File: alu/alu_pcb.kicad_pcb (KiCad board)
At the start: 2 copper layers, 115.6 x 86.4 mm, 56 parts, among them J1 Conn_02x03_Odd_Even, J2 Conn_02x02_Odd_Even, J3 Conn_02x08_Odd_Even, J4 Conn_02x08_Odd_Even, J5 Conn_02x08_Odd_Even, J6 Conn_02x08_Odd_Even, U1 74LS283, U10 74LS386, U11 74LS02, U12 74LS08, U13 74LS08, U14 74LS02, U15 74LS00, U2 74LS283, U3 74LS244, U4 74LS283, U5 74LS244, U6 74LS283, U7 74LS386, U8 74LS386, U9 74LS386

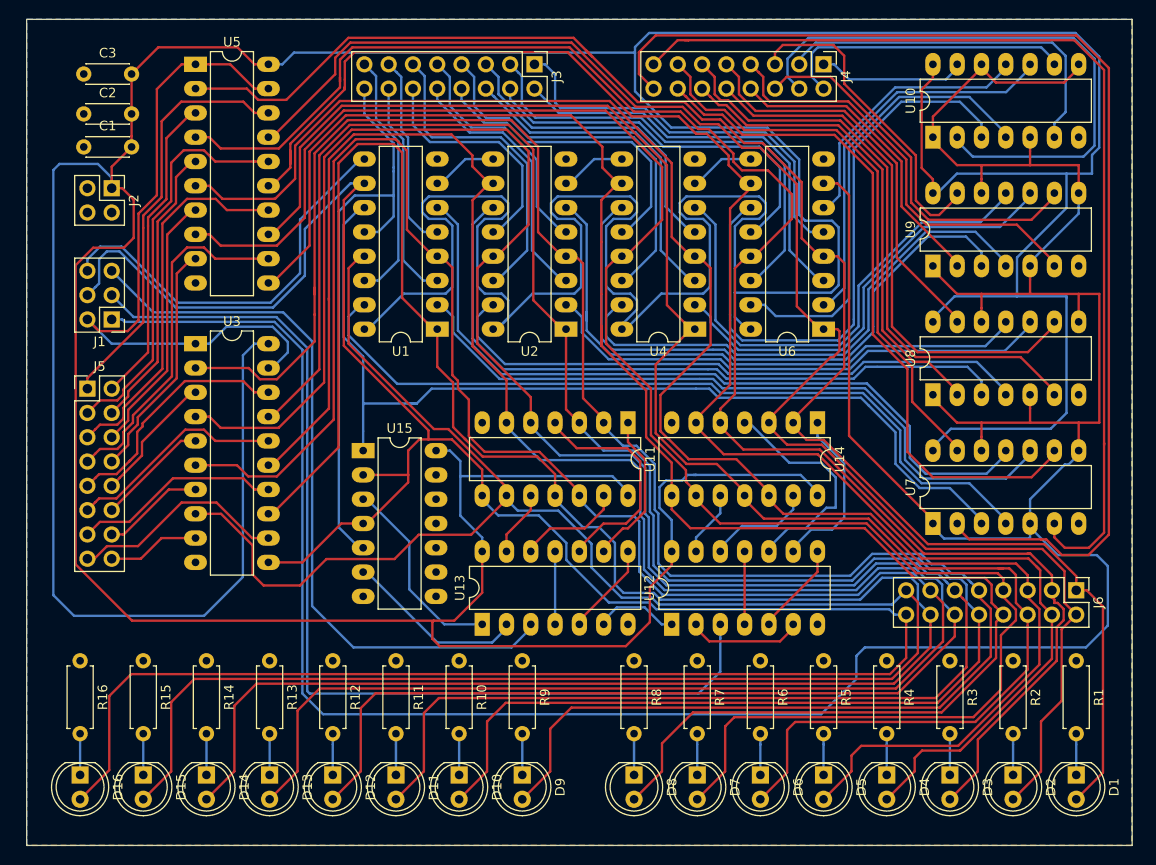
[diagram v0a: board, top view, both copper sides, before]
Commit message: route alu, upde register
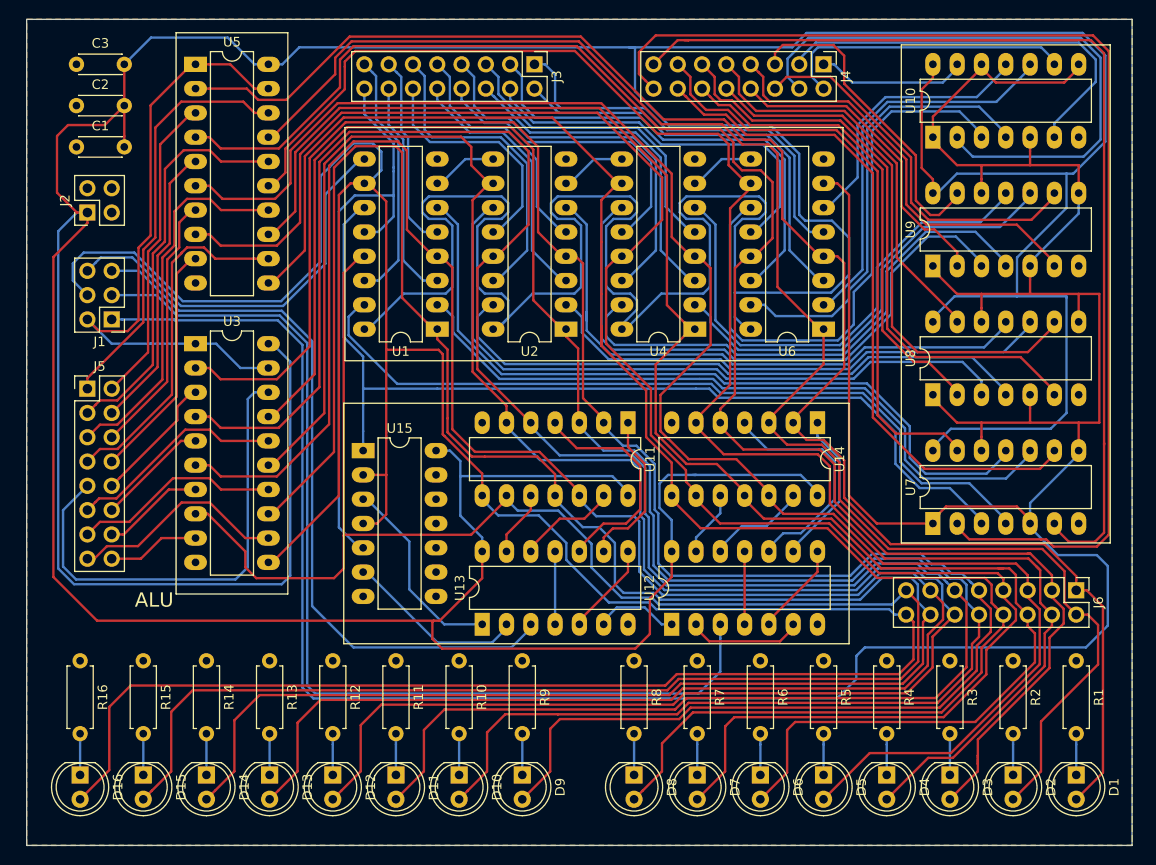
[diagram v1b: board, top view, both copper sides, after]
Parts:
- moved J2 3.59 mm to (43.2, 92.6), turned to 90 degrees
- moved C3 1.27 mm to (42.0, 77.1)
- moved C2 1.16 mm to (42.0, 81.4)
- moved C1 0.76 mm to (42.0, 85.7)
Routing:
- net /ALU/LTF: track 265.2 -> 316.8 mm
- net /CONN BUS DATA/D8: track 25.6 -> 49.9 mm
- net /ALU/~ENALBE_OUTPUT~: track 72.6 -> 65.8 mm
- net /CONN BUS B/D2: track 38.7 -> 42.9 mm
- net /CONN BUS SUM/D1: track 162.2 -> 165.5 mm
- net /CONN BUS B/D12: track 59.2 -> 62.2 mm
- net /CONN BUS SUM/D14: track 222.6 -> 219.8 mm
- net /CONN BUS SUM/D6: track 190.9 -> 188.2 mm
- net /CONN BUS SUM/D0: track 166.7 -> 168.9 mm
- net VCC: track 711.5 -> 713.6 mm
- net /CONN BUS SUM/D7: track 185.7 -> 183.6 mm
- net /CONN BUS SUM/D4: track 176.0 -> 174.2 mm
- net Net-(U12-Pad9): track 18.1 -> 16.4 mm
- net /ALU/D_BI3: track 64.0 -> 62.5 mm
- net /ALU/D_BI15: track 101.4 -> 100.0 mm
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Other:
- board text added: "ALU"

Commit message: ram pcb
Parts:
- removed the D1 at (146.6, 151.4)
- added C4: 0.1µF, Capacitor_THT:C_Disc_D4.3mm_W1.9mm_P5.00mm, F.Cu at (42.0, 83.3)
- added C5: 0.1µF, Capacitor_THT:C_Disc_D4.3mm_W1.9mm_P5.00mm, F.Cu at (42.0, 85.9)
- added D0: LED_ALT, LED_THT:LED_D5.0mm, F.Cu at (146.6, 151.4)
- R0: renamed from R1; value 220 -> 5k
- R1: renamed from R2; value 220 -> 5k
- R10: renamed from R11; value 220 -> 5k
- R11: renamed from R12; value 220 -> 5k
- R12: renamed from R13; value 220 -> 5k
- R13: renamed from R14; value 220 -> 5k
- R14: renamed from R15; value 220 -> 5k
- R15: renamed from R16; value 220 -> 5k
- R2: renamed from R3; value 220 -> 5k
- R3: renamed from R4; value 220 -> 5k
- R4: renamed from R5; value 220 -> 5k
- R5: renamed from R6; value 220 -> 5k
- R6: renamed from R7; value 220 -> 5k
- R7: renamed from R8; value 220 -> 5k
- R8: renamed from R9; value 220 -> 5k
- R9: renamed from R10; value 220 -> 5k
- moved C1 10.0 mm to (42.0, 75.7)
- moved C3 3.68 mm to (42.0, 80.8)
- moved C2 3.17 mm to (42.0, 78.2)
- renumbered D2 to D1, D11 to D10, D12 to D11, D13 to D12, D14 to D13, D15 to D14, D16 to D15, D3 to D2, D4 to D3, D5 to D4, D6 to D5, D7 to D6, D8 to D7, D9 to D8, D10 to D9
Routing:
- net VCC: track 713.6 -> 709.2 mm
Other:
- board size 115.6 x 86.4 mm -> 116.8 x 85.1 mm
- board text added: "BUS"
- board text added: "CO"
- board text added: "GND"
- board text added: "INPUT A"
- board text added: "INPUT B"
- board text added: "LTF"
- board text added: "OUT"
- board text added: "OVF"
- board text added: "PWR"
- board text added: "SUB"
- board text added: "ZF"
- board text added: "~EO~"

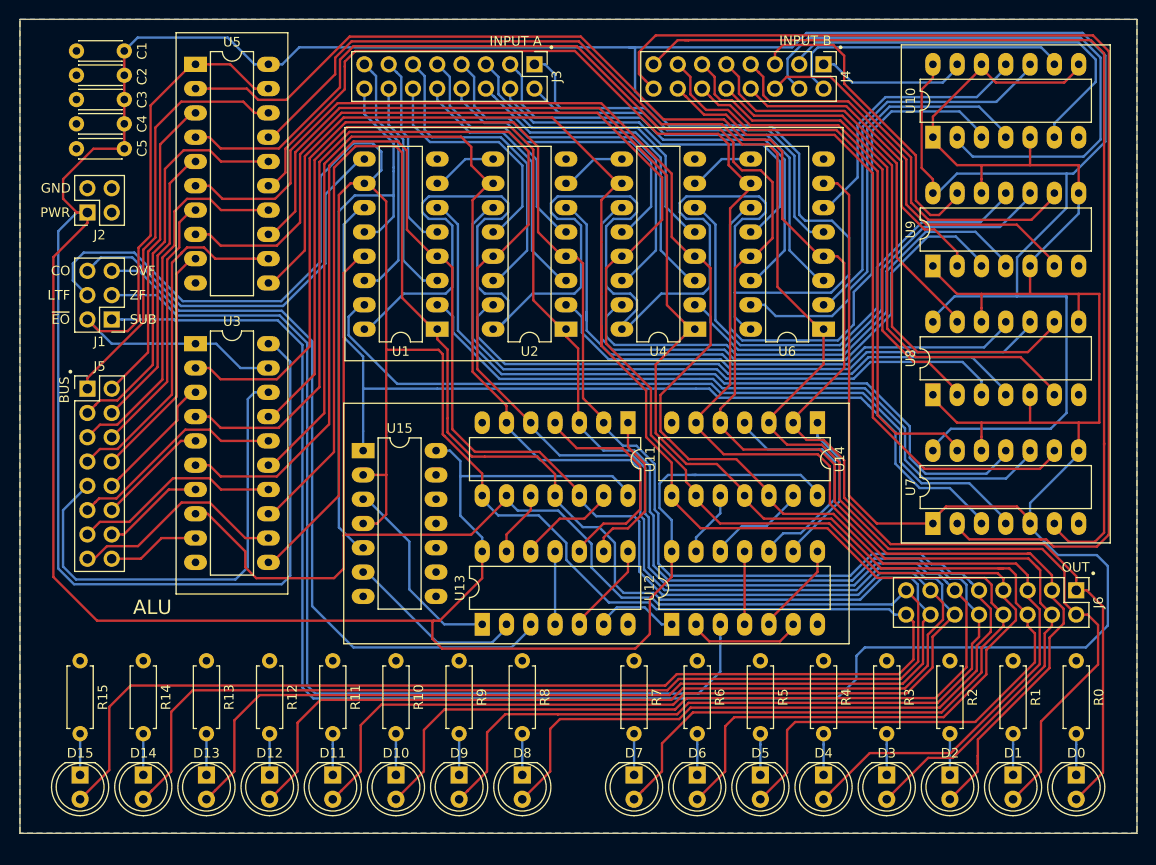
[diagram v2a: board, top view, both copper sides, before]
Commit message: add bit operations
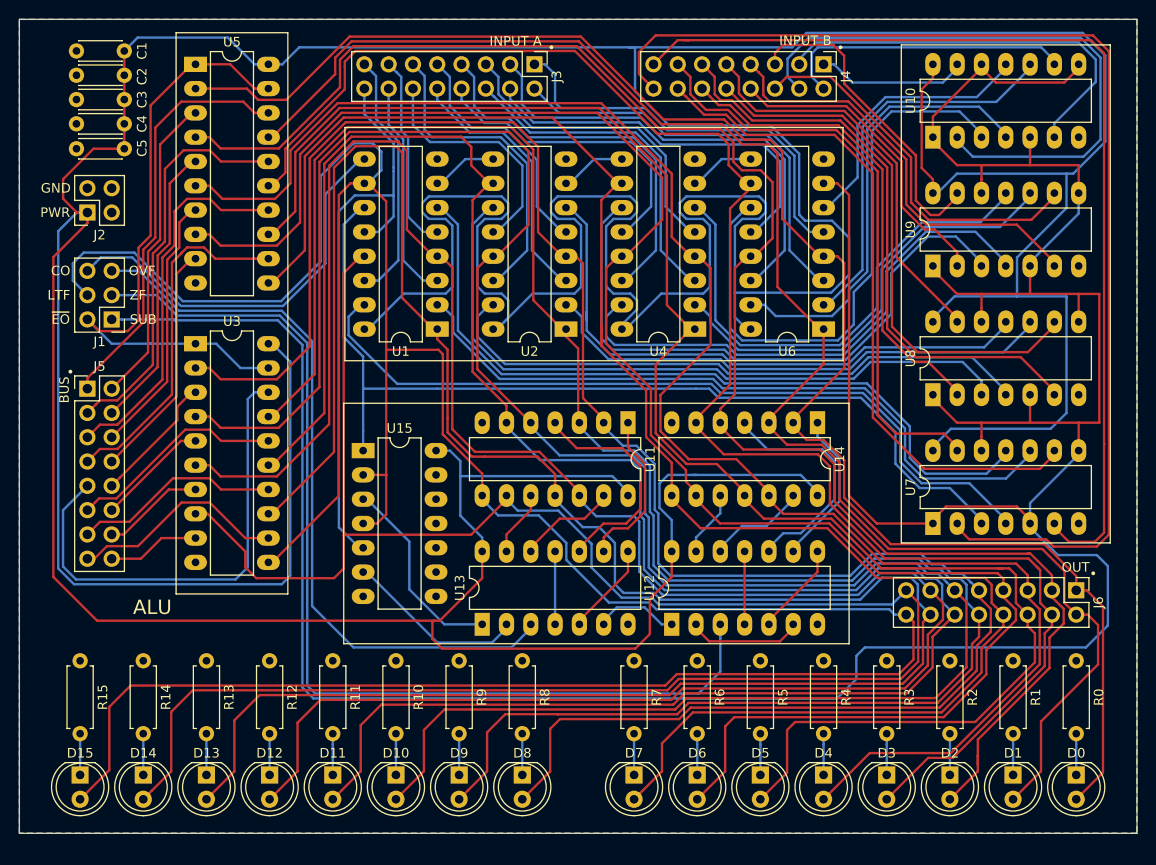
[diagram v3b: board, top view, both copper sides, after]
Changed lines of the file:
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@@
     (effects (font (size 1.5 1.5) (thickness 0.3)))
   )
-  (gr_line (start 36.1315 72.39) (end 36.1315 157.48) (layer Edge.Cuts) (width 0.05))
-  (gr_line (start 152.908 72.39) (end 36.1315 72.39) (layer Edge.Cuts) (width 0.05))
+  (gr_line (start 36.068 72.39) (end 36.068 157.48) (layer Edge.Cuts) (width 0.05))
+  (gr_line (start 152.908 72.39) (end 36.068 72.39) (layer Edge.Cuts) (width 0.05))
   (gr_line (start 152.908 157.48) (end 152.908 72.39) (layer Edge.Cuts) (width 0.05))
-  (gr_line (start 36.1315 157.48) (end 152.908 157.48) (layer Edge.Cuts) (width 0.05))
+  (gr_line (start 36.068 157.48) (end 152.908 157.48) (layer Edge.Cuts) (width 0.05))
   (segment (start 131.572 78.539) (end 131.572 77.089) (width 0.25) (layer F.Cu) (net 1))
   (segment (start 130.396999 79.714001) (end 131.572 78.539) (width 0.25) (layer F.Cu) (net 1))
@@
     (polygon
       (pts
-        (xy 36.1315 72.39) (xy 152.908 72.39) (xy 152.908 157.48) (xy 36.1315 157.48)
+        (xy 36.068 72.39) (xy 152.908 72.39) (xy 152.908 157.48) (xy 36.068 157.48)
       )
     )
@@
     (polygon
       (pts
-        (xy 36.1315 72.39) (xy 152.908 72.39) (xy 152.908 157.48) (xy 36.1315 157.48)
+        (xy 36.068 72.39) (xy 152.908 72.39) (xy 152.908 157.48) (xy 36.068 157.48)
       )
     )
